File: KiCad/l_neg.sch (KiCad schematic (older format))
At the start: 14 parts

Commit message: first commit
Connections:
- net OUT: no longer R?.2
- new net LED: R?.2
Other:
- moved on the sheet: R?
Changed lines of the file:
@@
 $Descr A4 11693 8268
 encoding utf-8
-Sheet 3 8
+Sheet 4 4
 Title ""
 Date ""
@@
 AR Path="/604C8E92/6067743B/605CA6A1" Ref="R?"  Part="1"
 AR Path="/604C8E92/6069EF2E/605CA6A1" Ref="R?"  Part="1"
+AR Path="/604C8E92/6087180E/605CA6A1" Ref="R?"  Part="1"
 F 0 "R?" H 4459 3946 50  0000 L CNN
 F 1 "10k" H 4459 3855 50  0000 L CNN
@@
 AR Path="/604C8E92/6067743B/605D57B8" Ref="C?"  Part="1"
 AR Path="/604C8E92/6069EF2E/605D57B8" Ref="C?"  Part="1"
+AR Path="/604C8E92/6087180E/605D57B8" Ref="C?"  Part="1"
 F 0 "C?" H 4492 4946 50  0000 L CNN
 F 1 "470n" H 4492 4855 50  0000 L CNN
@@
 AR Path="/604C8E92/6067743B/605D5FB7" Ref="SW?"  Part="1"
 AR Path="/604C8E92/6069EF2E/605D5FB7" Ref="SW?"  Part="1"
+AR Path="/604C8E92/6087180E/605D5FB7" Ref="SW?"  Part="1"
 F 0 "SW?" H 5700 4835 50  0000 C CNN
 F 1 "SW_Push_LED" H 5700 4744 50  0000 C CNN
@@
 AR Path="/604C8E92/6067743B/605D8BBC" Ref="R?"  Part="1"
 AR Path="/604C8E92/6069EF2E/605D8BBC" Ref="R?"  Part="1"
+AR Path="/604C8E92/6087180E/605D8BBC" Ref="R?"  Part="1"
 F 0 "R?" H 4459 2946 50  0000 L CNN
 F 1 "10k" H 4459 2855 50  0000 L CNN
@@
 AR Path="/604C8E92/6067743B/605D9138" Ref="#PWR?"  Part="1"
 AR Path="/604C8E92/6069EF2E/605D9138" Ref="#PWR?"  Part="1"
+AR Path="/604C8E92/6087180E/605D9138" Ref="#PWR?"  Part="1"
 F 0 "#PWR?" H 4400 5100 50  0001 C CNN
 F 1 "GND" H 4405 5177 50  0000 C CNN
@@
 AR Path="/604C8E92/6067743B/605D988B" Ref="R?"  Part="1"
 AR Path="/604C8E92/6069EF2E/605D988B" Ref="R?"  Part="1"
+AR Path="/604C8E92/6087180E/605D988B" Ref="R?"  Part="1"
 F 0 "R?" V 5904 3650 50  0000 C CNN
 F 1 "10k" V 5995 3650 50  0000 C CNN
@@
 AR Path="/604C8E92/6067743B/605DA2A0" Ref="R?"  Part="1"
 AR Path="/604C8E92/6069EF2E/605DA2A0" Ref="R?"  Part="1"
+AR Path="/604C8E92/6087180E/605DA2A0" Ref="R?"  Part="1"
 F 0 "R?" H 6391 4196 50  0000 R CNN
 F 1 "10k" H 6391 4105 50  0000 R CNN
@@
 AR Path="/604C8E92/6067743B/605DAF7B" Ref="R?"  Part="1"
 AR Path="/604C8E92/6069EF2E/605DAF7B" Ref="R?"  Part="1"
+AR Path="/604C8E92/6087180E/605DAF7B" Ref="R?"  Part="1"
 F 0 "R?" H 6509 4946 50  0000 L CNN
 F 1 "470k" H 6509 4855 50  0000 L CNN
@@
 AR Path="/604C8E92/6067743B/605DB9E1" Ref="R?"  Part="1"
 AR Path="/604C8E92/6069EF2E/605DB9E1" Ref="R?"  Part="1"
+AR Path="/604C8E92/6087180E/605DB9E1" Ref="R?"  Part="1"
 F 0 "R?" V 6704 4550 50  0000 C CNN
 F 1 "10k" V 6795 4550 50  0000 C CNN
@@
 AR Path="/604C8E92/6067743B/605DDA9F" Ref="R?"  Part="1"
 AR Path="/604C8E92/6069EF2E/605DDA9F" Ref="R?"  Part="1"
+AR Path="/604C8E92/6087180E/605DDA9F" Ref="R?"  Part="1"
 F 0 "R?" H 7491 4046 50  0000 R CNN
 F 1 "100k" H 7491 3955 50  0000 R CNN
@@
 AR Path="/604C8E92/6067743B/605DF842" Ref="R?"  Part="1"
 AR Path="/604C8E92/6069EF2E/605DF842" Ref="R?"  Part="1"
+AR Path="/604C8E92/6087180E/605DF842" Ref="R?"  Part="1"
 F 0 "R?" H 7491 2996 50  0000 R CNN
 F 1 "1M" H 7491 2905 50  0000 R CNN
@@
 Wire Wire Line
 	4950 5250 4400 5250
-Wire Wire Line
-	7250 4450 7250 3600
-Wire Wire Line
-	7250 3600 7550 3600
 Connection ~ 7550 3600
 Wire Wire Line
@@
 L Device:R_Small R?
 U 1 1 605E2C4C
-P 6150 4450
+P 6050 4450
 AR Path="/605C72FC/605E2C4C" Ref="R?"  Part="1"
 AR Path="/605ED2C3/605E2C4C" Ref="R?"  Part="1"
@@
 AR Path="/604C8E92/6067743B/605E2C4C" Ref="R?"  Part="1"
 AR Path="/604C8E92/6069EF2E/605E2C4C" Ref="R?"  Part="1"
-F 0 "R?" V 5954 4450 50  0000 C CNN
-F 1 "220" V 6045 4450 50  0000 C CNN
-F 2 "" H 6150 4450 50  0001 C CNN
-F 3 "~" H 6150 4450 50  0001 C CNN
-	1    6150 4450
+AR Path="/604C8E92/6087180E/605E2C4C" Ref="R?"  Part="1"
+F 0 "R?" V 5854 4450 50  0000 C CNN
+F 1 "220" V 5945 4450 50  0000 C CNN
+F 2 "" H 6050 4450 50  0001 C CNN
+F 3 "~" H 6050 4450 50  0001 C CNN
+	1    6050 4450
 	0    -1   1    0
 $EndComp
@@
 AR Path="/604C8E92/6067743B/60669235" Ref="Q?"  Part="1"
 AR Path="/604C8E92/6069EF2E/60669235" Ref="Q?"  Part="1"
+AR Path="/604C8E92/6087180E/60669235" Ref="Q?"  Part="1"
 F 0 "Q?" H 5241 3696 50  0000 L CNN
 F 1 "Q_NPN_BCE" H 5241 3605 50  0000 L CNN
@@
 AR Path="/604C8E92/6067743B/605DC332" Ref="Q?"  Part="1"
 AR Path="/604C8E92/6069EF2E/605DC332" Ref="Q?"  Part="1"
+AR Path="/604C8E92/6087180E/605DC332" Ref="Q?"  Part="1"
 F 0 "Q?" H 6740 3204 50  0000 L CNN
 F 1 "Q_PNP_BCE" H 6740 3295 50  0000 L CNN
@@
 AR Path="/604C8E92/6067743B/6066A306" Ref="Q?"  Part="1"
 AR Path="/604C8E92/6069EF2E/6066A306" Ref="Q?"  Part="1"
+AR Path="/604C8E92/6087180E/6066A306" Ref="Q?"  Part="1"
 F 0 "Q?" H 7641 4596 50  0000 L CNN
 F 1 "Q_NPN_BCE" H 7641 4505 50  0000 L CNN
@@
 $EndComp
 Wire Wire Line
-	6050 4450 5900 4450
-Wire Wire Line
-	6250 4450 7250 4450
-Wire Wire Line
 	5500 4450 5350 4450
 Wire Wire Line
@@
 	4400 5350 4400 5250
 Connection ~ 4400 5250
+Text HLabel 6200 4450 2    50   Input ~ 0
+LED
+Wire Wire Line
+	5900 4450 5950 4450
+Wire Wire Line
+	6150 4450 6200 4450
 $EndSCHEMATC

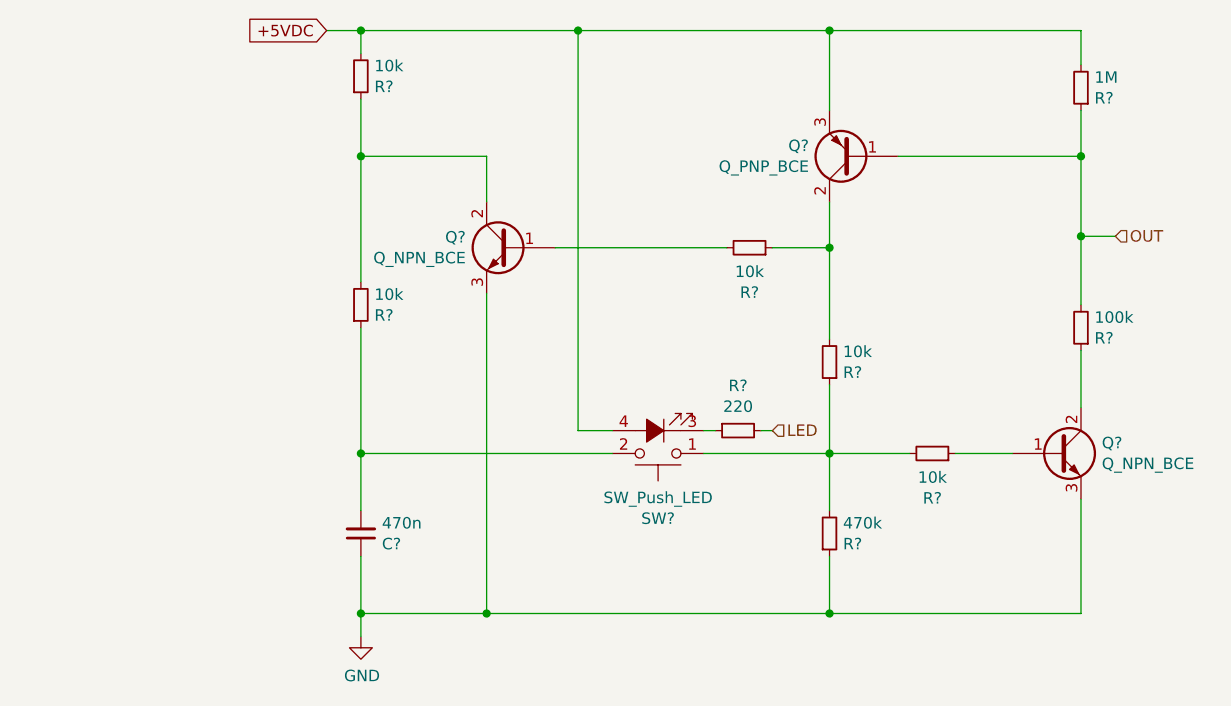
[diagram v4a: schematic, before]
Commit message: schematic completed
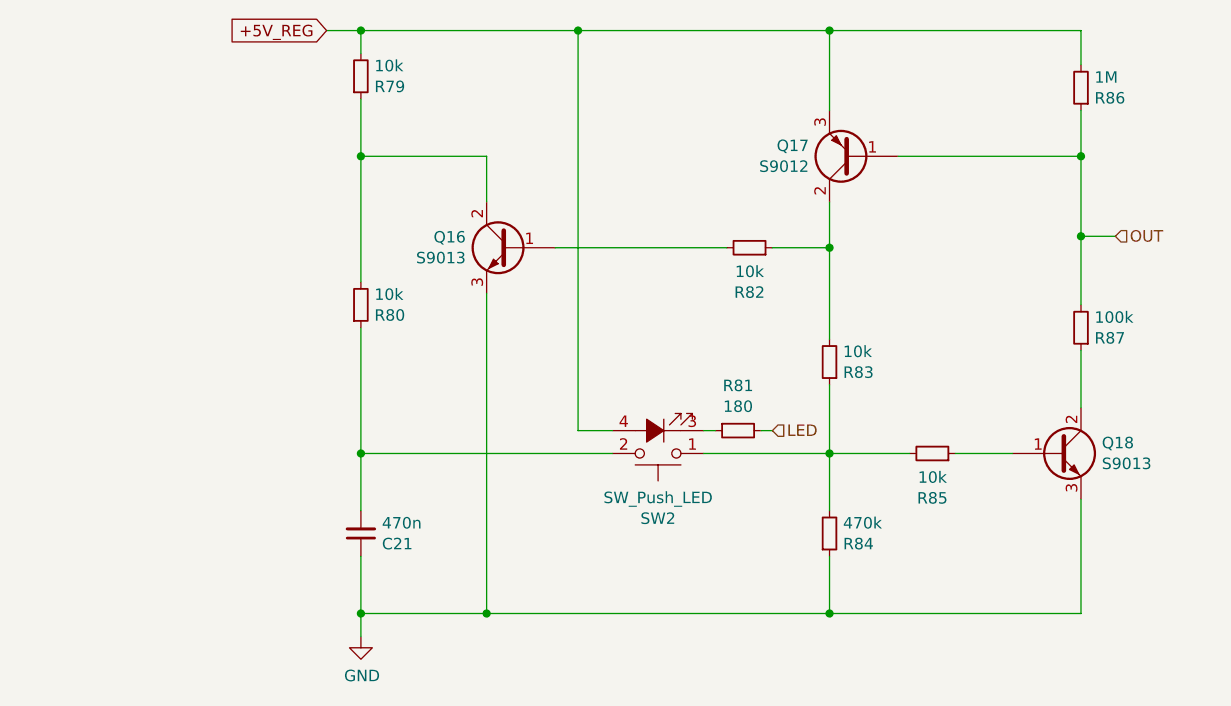
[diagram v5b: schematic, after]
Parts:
- Q16, Q18: renamed from Q?; value Q_NPN_BCE -> S9013
- Q17: renamed from Q?; value Q_PNP_BCE -> S9012
- R81: renamed from R?; value 220 -> 180
- gave numbers to parts that had none: 10
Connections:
- net +5VDC renamed +5V_REG
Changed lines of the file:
@@
 $Descr A4 11693 8268
 encoding utf-8
-Sheet 4 4
+Sheet 4 5
 Title ""
 Date ""
@@
 AR Path="/604C8E92/6069EF2E/605CA6A1" Ref="R?"  Part="1"
 AR Path="/604C8E92/6087180E/605CA6A1" Ref="R?"  Part="1"
-AR Path="/60AC1B12/605CA6A1" Ref="R?"  Part="1"
-AR Path="/60AC1B1E/605CA6A1" Ref="R?"  Part="1"
-F 0 "R?" H 4459 3946 50  0000 L CNN
+AR Path="/60AC1B12/605CA6A1" Ref="R80"  Part="1"
+AR Path="/60AC1B1E/605CA6A1" Ref="R71"  Part="1"
+F 0 "R80" H 4459 3946 50  0000 L CNN
 F 1 "10k" H 4459 3855 50  0000 L CNN
 F 2 "" H 4400 3900 50  0001 C CNN
@@
 AR Path="/604C8E92/6069EF2E/605D57B8" Ref="C?"  Part="1"
 AR Path="/604C8E92/6087180E/605D57B8" Ref="C?"  Part="1"
-AR Path="/60AC1B12/605D57B8" Ref="C?"  Part="1"
-AR Path="/60AC1B1E/605D57B8" Ref="C?"  Part="1"
-F 0 "C?" H 4492 4946 50  0000 L CNN
+AR Path="/60AC1B12/605D57B8" Ref="C21"  Part="1"
+AR Path="/60AC1B1E/605D57B8" Ref="C20"  Part="1"
+F 0 "C21" H 4492 4946 50  0000 L CNN
 F 1 "470n" H 4492 4855 50  0000 L CNN
 F 2 "" H 4400 4900 50  0001 C CNN
@@
 AR Path="/604C8E92/6069EF2E/605D5FB7" Ref="SW?"  Part="1"
 AR Path="/604C8E92/6087180E/605D5FB7" Ref="SW?"  Part="1"
-AR Path="/60AC1B12/605D5FB7" Ref="SW?"  Part="1"
-AR Path="/60AC1B1E/605D5FB7" Ref="SW?"  Part="1"
-F 0 "SW?" H 5700 4835 50  0000 C CNN
+AR Path="/60AC1B12/605D5FB7" Ref="SW2"  Part="1"
+AR Path="/60AC1B1E/605D5FB7" Ref="SW1"  Part="1"
+F 0 "SW2" H 5700 4835 50  0000 C CNN
 F 1 "SW_Push_LED" H 5700 4744 50  0000 C CNN
 F 2 "" H 5700 4750 50  0001 C CNN
@@
 AR Path="/604C8E92/6069EF2E/605D8BBC" Ref="R?"  Part="1"
 AR Path="/604C8E92/6087180E/605D8BBC" Ref="R?"  Part="1"
-AR Path="/60AC1B12/605D8BBC" Ref="R?"  Part="1"
-AR Path="/60AC1B1E/605D8BBC" Ref="R?"  Part="1"
-F 0 "R?" H 4459 2946 50  0000 L CNN
+AR Path="/60AC1B12/605D8BBC" Ref="R79"  Part="1"
+AR Path="/60AC1B1E/605D8BBC" Ref="R70"  Part="1"
+F 0 "R79" H 4459 2946 50  0000 L CNN
 F 1 "10k" H 4459 2855 50  0000 L CNN
 F 2 "" H 4400 2900 50  0001 C CNN
@@
 AR Path="/604C8E92/6069EF2E/605D9138" Ref="#PWR?"  Part="1"
 AR Path="/604C8E92/6087180E/605D9138" Ref="#PWR?"  Part="1"
-AR Path="/60AC1B12/605D9138" Ref="#PWR?"  Part="1"
-AR Path="/60AC1B1E/605D9138" Ref="#PWR?"  Part="1"
-F 0 "#PWR?" H 4400 5100 50  0001 C CNN
+AR Path="/60AC1B12/605D9138" Ref="#PWR033"  Part="1"
+AR Path="/60AC1B1E/605D9138" Ref="#PWR032"  Part="1"
+F 0 "#PWR033" H 4400 5100 50  0001 C CNN
 F 1 "GND" H 4405 5177 50  0000 C CNN
 F 2 "" H 4400 5350 50  0001 C CNN
@@
 AR Path="/604C8E92/6069EF2E/605D988B" Ref="R?"  Part="1"
 AR Path="/604C8E92/6087180E/605D988B" Ref="R?"  Part="1"
-AR Path="/60AC1B12/605D988B" Ref="R?"  Part="1"
-AR Path="/60AC1B1E/605D988B" Ref="R?"  Part="1"
-F 0 "R?" V 5904 3650 50  0000 C CNN
+AR Path="/60AC1B12/605D988B" Ref="R82"  Part="1"
+AR Path="/60AC1B1E/605D988B" Ref="R73"  Part="1"
+F 0 "R82" V 5904 3650 50  0000 C CNN
 F 1 "10k" V 5995 3650 50  0000 C CNN
 F 2 "" H 6100 3650 50  0001 C CNN
@@
 AR Path="/604C8E92/6069EF2E/605DA2A0" Ref="R?"  Part="1"
 AR Path="/604C8E92/6087180E/605DA2A0" Ref="R?"  Part="1"
-AR Path="/60AC1B12/605DA2A0" Ref="R?"  Part="1"
-AR Path="/60AC1B1E/605DA2A0" Ref="R?"  Part="1"
-F 0 "R?" H 6391 4196 50  0000 R CNN
+AR Path="/60AC1B12/605DA2A0" Ref="R83"  Part="1"
+AR Path="/60AC1B1E/605DA2A0" Ref="R74"  Part="1"
+F 0 "R83" H 6391 4196 50  0000 R CNN
 F 1 "10k" H 6391 4105 50  0000 R CNN
 F 2 "" H 6450 4150 50  0001 C CNN
@@
 AR Path="/604C8E92/6069EF2E/605DAF7B" Ref="R?"  Part="1"
 AR Path="/604C8E92/6087180E/605DAF7B" Ref="R?"  Part="1"
-AR Path="/60AC1B12/605DAF7B" Ref="R?"  Part="1"
-AR Path="/60AC1B1E/605DAF7B" Ref="R?"  Part="1"
-F 0 "R?" H 6509 4946 50  0000 L CNN
+AR Path="/60AC1B12/605DAF7B" Ref="R84"  Part="1"
+AR Path="/60AC1B1E/605DAF7B" Ref="R75"  Part="1"
+F 0 "R84" H 6509 4946 50  0000 L CNN
 F 1 "470k" H 6509 4855 50  0000 L CNN
 F 2 "" H 6450 4900 50  0001 C CNN
@@
 AR Path="/604C8E92/6069EF2E/605DB9E1" Ref="R?"  Part="1"
 AR Path="/604C8E92/6087180E/605DB9E1" Ref="R?"  Part="1"
-AR Path="/60AC1B12/605DB9E1" Ref="R?"  Part="1"
-AR Path="/60AC1B1E/605DB9E1" Ref="R?"  Part="1"
-F 0 "R?" V 6704 4550 50  0000 C CNN
+AR Path="/60AC1B12/605DB9E1" Ref="R85"  Part="1"
+AR Path="/60AC1B1E/605DB9E1" Ref="R76"  Part="1"
+F 0 "R85" V 6704 4550 50  0000 C CNN
 F 1 "10k" V 6795 4550 50  0000 C CNN
 F 2 "" H 6900 4550 50  0001 C CNN
@@
 AR Path="/604C8E92/6069EF2E/605DDA9F" Ref="R?"  Part="1"
 AR Path="/604C8E92/6087180E/605DDA9F" Ref="R?"  Part="1"
-AR Path="/60AC1B12/605DDA9F" Ref="R?"  Part="1"
-AR Path="/60AC1B1E/605DDA9F" Ref="R?"  Part="1"
-F 0 "R?" H 7491 4046 50  0000 R CNN
+AR Path="/60AC1B12/605DDA9F" Ref="R87"  Part="1"
+AR Path="/60AC1B1E/605DDA9F" Ref="R78"  Part="1"
+F 0 "R87" H 7491 4046 50  0000 R CNN
 F 1 "100k" H 7491 3955 50  0000 R CNN
 F 2 "" H 7550 4000 50  0001 C CNN
@@
 AR Path="/604C8E92/6069EF2E/605DF842" Ref="R?"  Part="1"
 AR Path="/604C8E92/6087180E/605DF842" Ref="R?"  Part="1"
-AR Path="/60AC1B12/605DF842" Ref="R?"  Part="1"
-AR Path="/60AC1B1E/605DF842" Ref="R?"  Part="1"
-F 0 "R?" H 7491 2996 50  0000 R CNN
+AR Path="/60AC1B12/605DF842" Ref="R86"  Part="1"
+AR Path="/60AC1B1E/605DF842" Ref="R77"  Part="1"
+F 0 "R86" H 7491 2996 50  0000 R CNN
 F 1 "1M" H 7491 2905 50  0000 R CNN
 F 2 "" H 7550 2950 50  0001 C CNN
@@
 AR Path="/604C8E92/6069EF2E/605E2C4C" Ref="R?"  Part="1"
 AR Path="/604C8E92/6087180E/605E2C4C" Ref="R?"  Part="1"
-AR Path="/60AC1B12/605E2C4C" Ref="R?"  Part="1"
-AR Path="/60AC1B1E/605E2C4C" Ref="R?"  Part="1"
-F 0 "R?" V 5854 4450 50  0000 C CNN
-F 1 "220" V 5945 4450 50  0000 C CNN
+AR Path="/60AC1B12/605E2C4C" Ref="R81"  Part="1"
+AR Path="/60AC1B1E/605E2C4C" Ref="R72"  Part="1"
+F 0 "R81" V 5854 4450 50  0000 C CNN
+F 1 "180" V 5945 4450 50  0000 C CNN
 F 2 "" H 6050 4450 50  0001 C CNN
 F 3 "~" H 6050 4450 50  0001 C CNN
@@
 Wire Wire Line
 	7700 3600 7550 3600
-Text GLabel 4250 2700 0    50   Input ~ 0
-+5VDC
 $Comp
 L Device:Q_NPN_BCE Q?
@@
 AR Path="/604C8E92/6069EF2E/60669235" Ref="Q?"  Part="1"
 AR Path="/604C8E92/6087180E/60669235" Ref="Q?"  Part="1"
-AR Path="/60AC1B12/60669235" Ref="Q?"  Part="1"
-AR Path="/60AC1B1E/60669235" Ref="Q?"  Part="1"
-F 0 "Q?" H 5241 3696 50  0000 L CNN
-F 1 "Q_NPN_BCE" H 5241 3605 50  0000 L CNN
+AR Path="/60AC1B12/60669235" Ref="Q16"  Part="1"
+AR Path="/60AC1B1E/60669235" Ref="Q13"  Part="1"
+F 0 "Q16" H 5241 3696 50  0000 L CNN
+F 1 "S9013" H 5241 3605 50  0000 L CNN
 F 2 "" H 5250 3750 50  0001 C CNN
 F 3 "~" H 5050 3650 50  0001 C CNN
@@
 AR Path="/604C8E92/6069EF2E/605DC332" Ref="Q?"  Part="1"
 AR Path="/604C8E92/6087180E/605DC332" Ref="Q?"  Part="1"
-AR Path="/60AC1B12/605DC332" Ref="Q?"  Part="1"
-AR Path="/60AC1B1E/605DC332" Ref="Q?"  Part="1"
-F 0 "Q?" H 6740 3204 50  0000 L CNN
-F 1 "Q_PNP_BCE" H 6740 3295 50  0000 L CNN
+AR Path="/60AC1B12/605DC332" Ref="Q17"  Part="1"
+AR Path="/60AC1B1E/605DC332" Ref="Q14"  Part="1"
+F 0 "Q17" H 6740 3204 50  0000 L CNN
+F 1 "S9012" H 6740 3295 50  0000 L CNN
 F 2 "" H 6750 3350 50  0001 C CNN
 F 3 "~" H 6550 3250 50  0001 C CNN
@@
 AR Path="/604C8E92/6069EF2E/6066A306" Ref="Q?"  Part="1"
 AR Path="/604C8E92/6087180E/6066A306" Ref="Q?"  Part="1"
-AR Path="/60AC1B12/6066A306" Ref="Q?"  Part="1"
-AR Path="/60AC1B1E/6066A306" Ref="Q?"  Part="1"
-F 0 "Q?" H 7641 4596 50  0000 L CNN
-F 1 "Q_NPN_BCE" H 7641 4505 50  0000 L CNN
+AR Path="/60AC1B12/6066A306" Ref="Q18"  Part="1"
+AR Path="/60AC1B1E/6066A306" Ref="Q15"  Part="1"
+F 0 "Q18" H 7641 4596 50  0000 L CNN
+F 1 "S9013" H 7641 4505 50  0000 L CNN
 F 2 "" H 7650 4650 50  0001 C CNN
 F 3 "~" H 7450 4550 50  0001 C CNN
@@
 Wire Wire Line
 	6150 4450 6200 4450
+Text GLabel 4250 2700 0    50   Input ~ 0
++5V_REG
 $EndSCHEMATC

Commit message: edited chez Gabri's
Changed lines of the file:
@@
 AR Path="/60AC1B12/605CA6A1" Ref="R80"  Part="1"
 AR Path="/60AC1B1E/605CA6A1" Ref="R71"  Part="1"
-F 0 "R80" H 4459 3946 50  0000 L CNN
+F 0 "R71" H 4459 3946 50  0000 L CNN
 F 1 "10k" H 4459 3855 50  0000 L CNN
 F 2 "" H 4400 3900 50  0001 C CNN
@@
 AR Path="/60AC1B12/605D57B8" Ref="C21"  Part="1"
 AR Path="/60AC1B1E/605D57B8" Ref="C20"  Part="1"
-F 0 "C21" H 4492 4946 50  0000 L CNN
+F 0 "C20" H 4492 4946 50  0000 L CNN
 F 1 "470n" H 4492 4855 50  0000 L CNN
 F 2 "" H 4400 4900 50  0001 C CNN
@@
 AR Path="/60AC1B12/605D5FB7" Ref="SW2"  Part="1"
 AR Path="/60AC1B1E/605D5FB7" Ref="SW1"  Part="1"
-F 0 "SW2" H 5700 4835 50  0000 C CNN
+F 0 "SW1" H 5700 4835 50  0000 C CNN
 F 1 "SW_Push_LED" H 5700 4744 50  0000 C CNN
 F 2 "" H 5700 4750 50  0001 C CNN
@@
 AR Path="/60AC1B12/605D8BBC" Ref="R79"  Part="1"
 AR Path="/60AC1B1E/605D8BBC" Ref="R70"  Part="1"
-F 0 "R79" H 4459 2946 50  0000 L CNN
+F 0 "R70" H 4459 2946 50  0000 L CNN
 F 1 "10k" H 4459 2855 50  0000 L CNN
 F 2 "" H 4400 2900 50  0001 C CNN
@@
 AR Path="/60AC1B12/605D9138" Ref="#PWR033"  Part="1"
 AR Path="/60AC1B1E/605D9138" Ref="#PWR032"  Part="1"
-F 0 "#PWR033" H 4400 5100 50  0001 C CNN
+F 0 "#PWR032" H 4400 5100 50  0001 C CNN
 F 1 "GND" H 4405 5177 50  0000 C CNN
 F 2 "" H 4400 5350 50  0001 C CNN
@@
 AR Path="/60AC1B12/605D988B" Ref="R82"  Part="1"
 AR Path="/60AC1B1E/605D988B" Ref="R73"  Part="1"
-F 0 "R82" V 5904 3650 50  0000 C CNN
+F 0 "R73" V 5904 3650 50  0000 C CNN
 F 1 "10k" V 5995 3650 50  0000 C CNN
 F 2 "" H 6100 3650 50  0001 C CNN
@@
 AR Path="/60AC1B12/605DA2A0" Ref="R83"  Part="1"
 AR Path="/60AC1B1E/605DA2A0" Ref="R74"  Part="1"
-F 0 "R83" H 6391 4196 50  0000 R CNN
+F 0 "R74" H 6391 4196 50  0000 R CNN
 F 1 "10k" H 6391 4105 50  0000 R CNN
 F 2 "" H 6450 4150 50  0001 C CNN
@@
 AR Path="/60AC1B12/605DAF7B" Ref="R84"  Part="1"
 AR Path="/60AC1B1E/605DAF7B" Ref="R75"  Part="1"
-F 0 "R84" H 6509 4946 50  0000 L CNN
+F 0 "R75" H 6509 4946 50  0000 L CNN
 F 1 "470k" H 6509 4855 50  0000 L CNN
 F 2 "" H 6450 4900 50  0001 C CNN
@@
 AR Path="/60AC1B12/605DB9E1" Ref="R85"  Part="1"
 AR Path="/60AC1B1E/605DB9E1" Ref="R76"  Part="1"
-F 0 "R85" V 6704 4550 50  0000 C CNN
+F 0 "R76" V 6704 4550 50  0000 C CNN
 F 1 "10k" V 6795 4550 50  0000 C CNN
 F 2 "" H 6900 4550 50  0001 C CNN
@@
 AR Path="/60AC1B12/605DDA9F" Ref="R87"  Part="1"
 AR Path="/60AC1B1E/605DDA9F" Ref="R78"  Part="1"
-F 0 "R87" H 7491 4046 50  0000 R CNN
+F 0 "R78" H 7491 4046 50  0000 R CNN
 F 1 "100k" H 7491 3955 50  0000 R CNN
 F 2 "" H 7550 4000 50  0001 C CNN
@@
 AR Path="/60AC1B12/605DF842" Ref="R86"  Part="1"
 AR Path="/60AC1B1E/605DF842" Ref="R77"  Part="1"
-F 0 "R86" H 7491 2996 50  0000 R CNN
+F 0 "R77" H 7491 2996 50  0000 R CNN
 F 1 "1M" H 7491 2905 50  0000 R CNN
 F 2 "" H 7550 2950 50  0001 C CNN
@@
 AR Path="/60AC1B12/605E2C4C" Ref="R81"  Part="1"
 AR Path="/60AC1B1E/605E2C4C" Ref="R72"  Part="1"
-F 0 "R81" V 5854 4450 50  0000 C CNN
+F 0 "R72" V 5854 4450 50  0000 C CNN
 F 1 "180" V 5945 4450 50  0000 C CNN
 F 2 "" H 6050 4450 50  0001 C CNN
@@
 AR Path="/60AC1B12/60669235" Ref="Q16"  Part="1"
 AR Path="/60AC1B1E/60669235" Ref="Q13"  Part="1"
-F 0 "Q16" H 5241 3696 50  0000 L CNN
+F 0 "Q13" H 5241 3696 50  0000 L CNN
 F 1 "S9013" H 5241 3605 50  0000 L CNN
 F 2 "" H 5250 3750 50  0001 C CNN
@@
 AR Path="/60AC1B12/605DC332" Ref="Q17"  Part="1"
 AR Path="/60AC1B1E/605DC332" Ref="Q14"  Part="1"
-F 0 "Q17" H 6740 3204 50  0000 L CNN
+F 0 "Q14" H 6740 3204 50  0000 L CNN
 F 1 "S9012" H 6740 3295 50  0000 L CNN
 F 2 "" H 6750 3350 50  0001 C CNN
@@
 AR Path="/60AC1B12/6066A306" Ref="Q18"  Part="1"
 AR Path="/60AC1B1E/6066A306" Ref="Q15"  Part="1"
-F 0 "Q18" H 7641 4596 50  0000 L CNN
+F 0 "Q15" H 7641 4596 50  0000 L CNN
 F 1 "S9013" H 7641 4505 50  0000 L CNN
 F 2 "" H 7650 4650 50  0001 C CNN

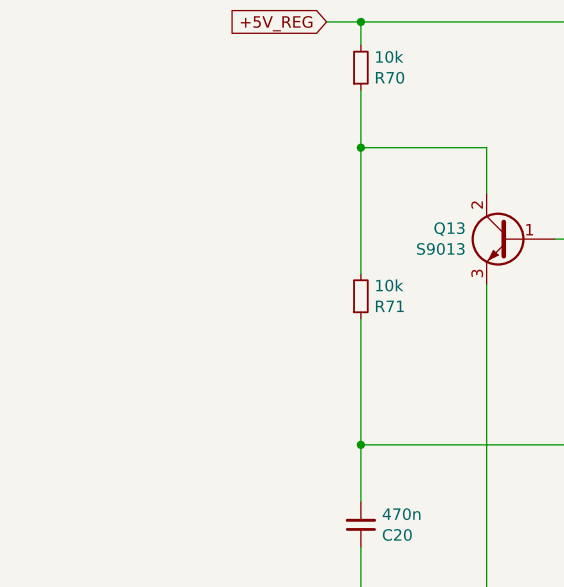
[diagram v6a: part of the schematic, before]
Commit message: added bom
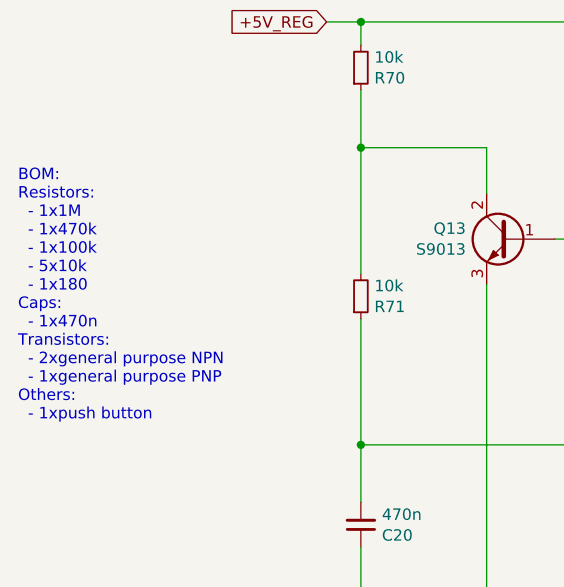
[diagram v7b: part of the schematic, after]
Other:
- note added: "BOM:\nResistors:\n - 1x1M\n - 1x470k\n - 1x100k\n - 5x10k\n - 1x180\nCaps:\n - 1x470n\nTransistors:\n - 2xgeneral purpose NPN\n - 1xgeneral purpose PNP\nOthers:\n - 1xpush button"
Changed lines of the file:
@@
 Text GLabel 4250 2700 0    50   Input ~ 0
 +5V_REG
+Text Notes 2900 4450 0    50   ~ 0
+BOM:\nResistors:\n  - 1x1M\n  - 1x470k\n  - 1x100k\n  - 5x10k\n  - 1x180\nCaps:\n  - 1x470n\nTransistors:\n  - 2xgeneral purpose NPN\n  - 1xgeneral purpose PNP\nOthers:\n  - 1xpush button
 $EndSCHEMATC
